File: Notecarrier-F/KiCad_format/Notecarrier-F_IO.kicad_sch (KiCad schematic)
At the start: 0 parts

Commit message: Port Notecarrier-F schematic and BOM.
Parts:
- added J10, J9: Conn_01x24, symbol Connector_Generic:Conn_01x24
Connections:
- new net F_3V3: J10.1 (F_3V3)
- new net F_A0: J9.23 (A0)
- new net F_A1: J9.22 (A1)
- new net F_A2: J9.21 (A2)
- new net F_A3: J9.20 (A3)
- new net F_A4: J9.19 (A4)
- new net F_A5: J9.18 (A5)
- new net F_AREF: J9.24 (AREF)
- new net F_B0_SW: J9.12 (B0)
- new net F_D10: J9.8 (10)
- new net F_D11: J9.9 (11)
- new net F_D12: J9.10 (12)
- new net F_D13: J9.11 (13)
- new net F_D5: J9.5
- new net F_D6: J9.6
- new net F_D9: J9.7 (9)
- new net F_EN: J9.2 (F_EN)
- new net F_MISO: J9.15 (MISO)
- new net F_MOSI: J9.16 (MOSI)
- new net F_NRST_SW: J9.1 (F_NRST)
- new net F_RX_SW: J9.14 (RX)
- new net F_SCK: J9.17 (SCK)
- new net F_SCL: J9.4 (SCL)
- new net F_SDA: J9.3 (SDA)
- new net F_TX_SW: J9.13 (TX)
- new net GND: J10.11 (GND), J10.24 (GND), J10.8 (GND)
- new net N_ATTN: J10.14 (N_ATTN)
- new net N_AUX1: J10.18 (N_AUX1)
- new net N_AUX2: J10.19 (N_AUX2)
- new net N_AUX3: J10.20 (N_AUX3)
- new net N_AUX4: J10.21 (N_AUX4)
- new net N_AUX_EN: J10.15 (N_AUXEN)
- new net N_AUX_RX: J10.16 (N_AUXRX)
- new net N_AUX_TX: J10.17 (N_AUXTX)
- new net N_EN: J10.9 (N_EN)
- new net N_NRST: J10.10 (N_NRST)
- new net N_RX: J10.22 (N_RX)
- new net N_SCL: J10.12 (N_SCL)
- new net N_SDA: J10.13 (N_SDA)
- new net N_TX: J10.23 (N_TX)
- new net N_VIO: J10.5 (VIO)
- new net V+: J10.7 (V+)
- new net VBAT: J10.3 (BAT)
- new net VMAIN: J10.4 (MAIN)
- new net VSOLAR: J10.6 (SOLAR)
- new net VUSB: J10.2 (VUSB)
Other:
- note added: "Label Promotion"
- note added: "Pin Headers"
- note added: "Several of the net labels on this sheet need to be common with other sheets. In the original Altium source files, this was achieved for some labels by adding Off-Sheet Connectors to the nets. But the remainder (inadvertently perhaps) rely on promoting all net labels to global using the "Net Identifier Scope" setting. This renders the original Off Sheet Connectors redundant. To avoid losing that d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"
- title: (none) -> Notecarrier-F

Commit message: Ported footprint assignments, board outline, copper layers and dimensional drawings for Notecarrier-F.
Footprints currently held in a “blues-kicad-lib-pending” library, prior to merging with “blues-kicad-lib” and deleting unused items.
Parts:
- J10, J9: footprint (none) -> blues-kicad-lib-pending:CES-124-01-S-S
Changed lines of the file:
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@@
       (effects (font (size 1.27 1.27)) hide)
     )
-    (property "Footprint" "" (at 139.7 218.44 0)
+    (property "Footprint" "blues-kicad-lib-pending:CES-124-01-S-S" (at 139.7 218.44 0)
       (effects (font (size 1.27 1.27)) hide)
     )
@@
       (effects (font (size 1.27 1.27)) hide)
     )
-    (property "Footprint" "" (at 63.5 218.44 0)
+    (property "Footprint" "blues-kicad-lib-pending:CES-124-01-S-S" (at 63.5 218.44 0)
       (effects (font (size 1.27 1.27)) hide)
     )

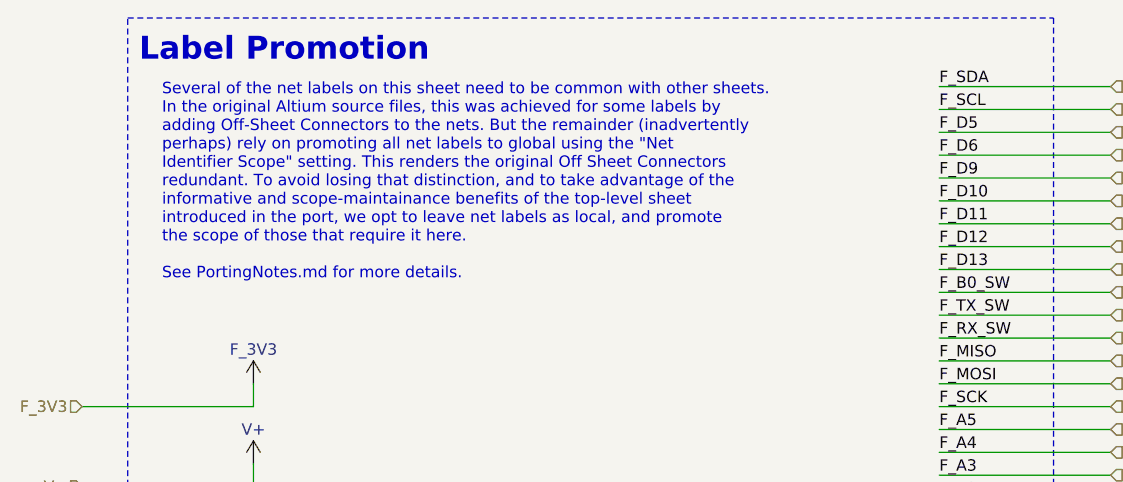
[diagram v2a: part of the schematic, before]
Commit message: Apply first pass validation of Notecarrier-F port
Huge push to identify, solve, document and revalidate all the details revealed by the first run of the validation process. Validation is now acceptable and preparation can be made to release Rev A.
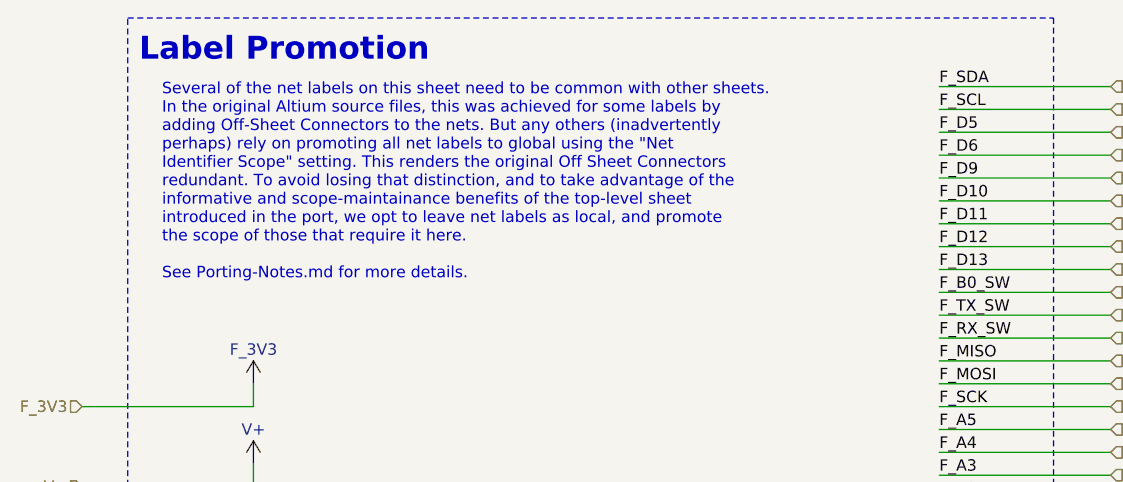
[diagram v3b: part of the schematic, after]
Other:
- note added: "Several of the net labels on this sheet need to be common with other sheets. In the original Altium source files, this was achieved for some labels by adding Off-Sheet Connectors to the nets. But any others (inadvertently perhaps) rely on promoting all net labels to global using the "Net Identifier Scope" setting. This renders the original Off Sheet Connectors redundant. To avoid losing that dist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"
- note removed: "Several of the net labels on this sheet need to be common with other sheets. In the original Altium source files, this was achieved for some labels by adding Off-Sheet Connectors to the nets. But the remainder (inadvertently perhaps) rely on promoting all net labels to global using the "Net Identifier Scope" setting. This renders the original Off Sheet Connectors redundant. To avoid losing that d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"
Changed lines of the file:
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@@
     (effects (font (size 2.54 2.54) (thickness 0.508) bold) (justify left bottom))
   )
-  (text "Several of the net labels on this sheet need to be common with other sheets.\nIn the original Altium source files, this was achieved for some labels by\nadding Off-Sheet Connectors to the nets. But the remainder (inadvertently\nperhaps) rely on promoting all net labels to global using the \"Net\nIdentifier Scope\" setting. This renders the original Off Sheet Connectors\nredundant. To avoid losing that distinction, and to take advantage of the\ninformative and scope-maintainance benefits of the top-level sheet\nintroduced in the port, we opt to leave net labels as local, and promote\nthe scope of those that require it here.\n\nSee PortingNotes.md for more details."
+  (text "Several of the net labels on this sheet need to be common with other sheets.\nIn the original Altium source files, this was achieved for some labels by\nadding Off-Sheet Connectors to the nets. But any others (inadvertently\nperhaps) rely on promoting all net labels to global using the \"Net\nIdentifier Scope\" setting. This renders the original Off Sheet Connectors\nredundant. To avoid losing that distinction, and to take advantage of the\ninformative and scope-maintainance benefits of the top-level sheet\nintroduced in the port, we opt to leave net labels as local, and promote\nthe scope of those that require it here.\n\nSee Porting-Notes.md for more details."
     (at 274.32 55.88 0)
     (effects (font (size 1.27 1.27)) (justify left bottom))

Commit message: Merge pending library into main.
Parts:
- J10, J9: footprint blues-kicad-lib-pending:CES-124-01-S-S -> blues-kicad-lib:CES-124-01-S-S
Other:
- moved on the sheet: J10, J9
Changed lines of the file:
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@@
     )
   )
-  (symbol (lib_name "Conn_01x24_1") (lib_id "Connector_Generic:Conn_01x24") (at 139.7 218.44 0) (mirror y) (unit 1)
+  (symbol (lib_id "Connector_Generic:Conn_01x24") (at 139.7 218.44 0) (mirror y) (unit 1)
     (in_bom yes) (on_board yes) (dnp no)
-    (property "Reference" "J10" (at 132.08 186.69 0)
+    (property "Reference" "J10" (at 139.7 187.96 0)
       (effects (font (size 1.27 1.27)))
     )
@@
       (effects (font (size 1.27 1.27)) hide)
     )
-    (property "Footprint" "blues-kicad-lib-pending:CES-124-01-S-S" (at 139.7 218.44 0)
+    (property "Footprint" "blues-kicad-lib:CES-124-01-S-S" (at 139.7 218.44 0)
       (effects (font (size 1.27 1.27)) hide)
     )
@@
       (effects (font (size 1.27 1.27)) hide)
     )
-    (property "Order Code" "SAM1085-24-ND" (at 129.54 252.73 0)
+    (property "Order Code" "SAM1085-24-ND" (at 138.43 251.46 0)
       (effects (font (size 1.27 1.27)) (justify right))
     )
@@
   (symbol (lib_id "Connector_Generic:Conn_01x24") (at 63.5 218.44 0) (mirror y) (unit 1)
     (in_bom yes) (on_board yes) (dnp no)
-    (property "Reference" "J9" (at 55.88 186.69 0)
+    (property "Reference" "J9" (at 63.5 187.96 0)
       (effects (font (size 1.27 1.27)))
     )
@@
       (effects (font (size 1.27 1.27)) hide)
     )
-    (property "Footprint" "blues-kicad-lib-pending:CES-124-01-S-S" (at 63.5 218.44 0)
+    (property "Footprint" "blues-kicad-lib:CES-124-01-S-S" (at 63.5 218.44 0)
       (effects (font (size 1.27 1.27)) hide)
     )
@@
       (effects (font (size 1.27 1.27)) hide)
     )
-    (property "Order Code" "SAM1085-24-ND" (at 54.61 252.73 0)
+    (property "Order Code" "SAM1085-24-ND" (at 62.23 251.46 0)
       (effects (font (size 1.27 1.27)) (justify right))
     )
